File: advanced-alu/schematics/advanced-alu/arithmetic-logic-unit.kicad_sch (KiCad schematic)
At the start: 5 parts

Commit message: updated ALU design
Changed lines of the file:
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@@
     (stroke (width 0) (type default) (color 0 0 0 0))
   )
-  (bus_entry (at 213.36 53.34) (size 2.54 2.54)
-    (stroke (width 0) (type default) (color 0 0 0 0))
-  )
-  (bus_entry (at 210.82 53.34) (size 2.54 2.54)
-    (stroke (width 0) (type default) (color 0 0 0 0))
-  )
-  (bus_entry (at 208.28 53.34) (size 2.54 2.54)
-    (stroke (width 0) (type default) (color 0 0 0 0))
-  )
-  (bus_entry (at 205.74 53.34) (size 2.54 2.54)
-    (stroke (width 0) (type default) (color 0 0 0 0))
-  )
-  (bus_entry (at 146.685 53.34) (size 2.54 2.54)
-    (stroke (width 0) (type default) (color 0 0 0 0))
-  )
-  (bus_entry (at 144.145 53.34) (size 2.54 2.54)
-    (stroke (width 0) (type default) (color 0 0 0 0))
-  )
-  (bus_entry (at 149.225 53.34) (size 2.54 2.54)
-    (stroke (width 0) (type default) (color 0 0 0 0))
-  )
-  (bus_entry (at 151.765 53.34) (size 2.54 2.54)
+  (bus_entry (at 213.36 63.5) (size 2.54 2.54)
+    (stroke (width 0) (type default) (color 0 0 0 0))
+  )
+  (bus_entry (at 210.82 63.5) (size 2.54 2.54)
+    (stroke (width 0) (type default) (color 0 0 0 0))
+  )
+  (bus_entry (at 208.28 63.5) (size 2.54 2.54)
+    (stroke (width 0) (type default) (color 0 0 0 0))
+  )
+  (bus_entry (at 205.74 63.5) (size 2.54 2.54)
+    (stroke (width 0) (type default) (color 0 0 0 0))
+  )
+  (bus_entry (at 146.685 63.5) (size 2.54 2.54)
+    (stroke (width 0) (type default) (color 0 0 0 0))
+  )
+  (bus_entry (at 144.145 63.5) (size 2.54 2.54)
+    (stroke (width 0) (type default) (color 0 0 0 0))
+  )
+  (bus_entry (at 149.225 63.5) (size 2.54 2.54)
+    (stroke (width 0) (type default) (color 0 0 0 0))
+  )
+  (bus_entry (at 151.765 63.5) (size 2.54 2.54)
     (stroke (width 0) (type default) (color 0 0 0 0))
   )
@@
     (stroke (width 0) (type default) (color 0 0 0 0))
   )
-  (bus (pts (xy 151.765 53.34) (xy 205.74 53.34))
+  (bus (pts (xy 151.765 63.5) (xy 205.74 63.5))
     (stroke (width 0) (type default) (color 0 0 0 0))
   )
@@
     (stroke (width 0) (type default) (color 0 0 0 0))
   )
-  (bus (pts (xy 146.685 53.34) (xy 149.225 53.34))
+  (bus (pts (xy 146.685 63.5) (xy 149.225 63.5))
     (stroke (width 0) (type default) (color 0 0 0 0))
   )
@@
     (stroke (width 0) (type default) (color 0 0 0 0))
   )
-  (wire (pts (xy 151.765 55.88) (xy 151.765 84.455))
+  (wire (pts (xy 151.765 66.04) (xy 151.765 84.455))
     (stroke (width 0) (type default) (color 0 0 0 0))
   )
@@
     (stroke (width 0) (type default) (color 0 0 0 0))
   )
-  (bus (pts (xy 208.28 53.34) (xy 210.82 53.34))
+  (bus (pts (xy 208.28 63.5) (xy 210.82 63.5))
     (stroke (width 0) (type default) (color 0 0 0 0))
   )
@@
     (stroke (width 0) (type default) (color 0 0 0 0))
   )
-  (bus (pts (xy 144.145 53.34) (xy 146.685 53.34))
-    (stroke (width 0) (type default) (color 0 0 0 0))
-  )
-  (wire (pts (xy 146.685 55.88) (xy 146.685 84.455))
+  (bus (pts (xy 144.145 63.5) (xy 146.685 63.5))
+    (stroke (width 0) (type default) (color 0 0 0 0))
+  )
+  (wire (pts (xy 146.685 66.04) (xy 146.685 84.455))
     (stroke (width 0) (type default) (color 0 0 0 0))
   )
@@
     (stroke (width 0) (type default) (color 0 0 0 0))
   )
-  (bus (pts (xy 210.82 53.34) (xy 213.36 53.34))
+  (bus (pts (xy 210.82 63.5) (xy 213.36 63.5))
     (stroke (width 0) (type default) (color 0 0 0 0))
   )
@@
     (stroke (width 0) (type default) (color 0 0 0 0))
   )
-  (bus (pts (xy 52.07 53.34) (xy 144.145 53.34))
+  (bus (pts (xy 52.07 63.5) (xy 144.145 63.5))
     (stroke (width 0) (type default) (color 0 0 0 0))
   )
@@
     (stroke (width 0) (type default) (color 0 0 0 0))
   )
-  (wire (pts (xy 210.82 55.88) (xy 210.82 84.455))
+  (wire (pts (xy 210.82 66.04) (xy 210.82 84.455))
     (stroke (width 0) (type default) (color 0 0 0 0))
   )
@@
     (stroke (width 0) (type default) (color 0 0 0 0))
   )
-  (wire (pts (xy 213.36 55.88) (xy 213.36 84.455))
+  (wire (pts (xy 213.36 66.04) (xy 213.36 84.455))
     (stroke (width 0) (type default) (color 0 0 0 0))
   )
@@
     (stroke (width 0) (type default) (color 0 0 0 0))
   )
-  (wire (pts (xy 215.9 55.88) (xy 215.9 84.455))
-    (stroke (width 0) (type default) (color 0 0 0 0))
-  )
-  (bus (pts (xy 205.74 53.34) (xy 208.28 53.34))
+  (wire (pts (xy 215.9 66.04) (xy 215.9 84.455))
+    (stroke (width 0) (type default) (color 0 0 0 0))
+  )
+  (bus (pts (xy 205.74 63.5) (xy 208.28 63.5))
     (stroke (width 0) (type default) (color 0 0 0 0))
   )
@@
     (stroke (width 0) (type default) (color 0 0 0 0))
   )
-  (bus (pts (xy 149.225 53.34) (xy 151.765 53.34))
+  (bus (pts (xy 149.225 63.5) (xy 151.765 63.5))
     (stroke (width 0) (type default) (color 0 0 0 0))
   )
@@
     (stroke (width 0) (type default) (color 0 0 0 0))
   )
-  (wire (pts (xy 208.28 55.88) (xy 208.28 84.455))
+  (wire (pts (xy 208.28 66.04) (xy 208.28 84.455))
     (stroke (width 0) (type default) (color 0 0 0 0))
   )
@@
     (stroke (width 0) (type default) (color 0 0 0 0))
   )
-  (wire (pts (xy 149.225 55.88) (xy 149.225 84.455))
+  (wire (pts (xy 149.225 66.04) (xy 149.225 84.455))
     (stroke (width 0) (type default) (color 0 0 0 0))
   )
@@
     (stroke (width 0) (type default) (color 0 0 0 0))
   )
-  (wire (pts (xy 154.305 55.88) (xy 154.305 84.455))
+  (wire (pts (xy 154.305 66.04) (xy 154.305 84.455))
     (stroke (width 0) (type default) (color 0 0 0 0))
   )
@@
     (effects (font (size 1.27 1.27)) (justify right))
   )
-  (hierarchical_label "LO_TMP_[0..7]" (shape input) (at 52.07 53.34 180)
+  (hierarchical_label "LO_TMP_[0..7]" (shape input) (at 52.07 63.5 180)
     (effects (font (size 1.27 1.27)) (justify right))
   )
@@
       (effects (font (size 1.27 1.27)) hide)
     )
+    (pin "1")
+    (pin "2")
     (pin "3")
     (pin "4")
+    (pin "5")
+    (pin "6")
+    (pin "8")
+    (pin "9")
+    (pin "10")
+    (pin "11")
+    (pin "12")
+    (pin "13")
+    (pin "14")
+    (pin "7")
   )
   (symbol (lib_id "74xx:74LS245") (at 101.6 95.25 270) (mirror x) (unit 1)

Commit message: updated documentation
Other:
- title: (none) -> Advanced Arithmetic Logic Unit - ALU
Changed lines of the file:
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@@
 (kicad_sch (version 20211123) (generator eeschema)
   (paper "A4")
+  (title_block
+    (title "Advanced Arithmetic Logic Unit - ALU")
+  )
   (junction (at 156.21 167.005) (diameter 0) (color 0 0 0 0)
   )

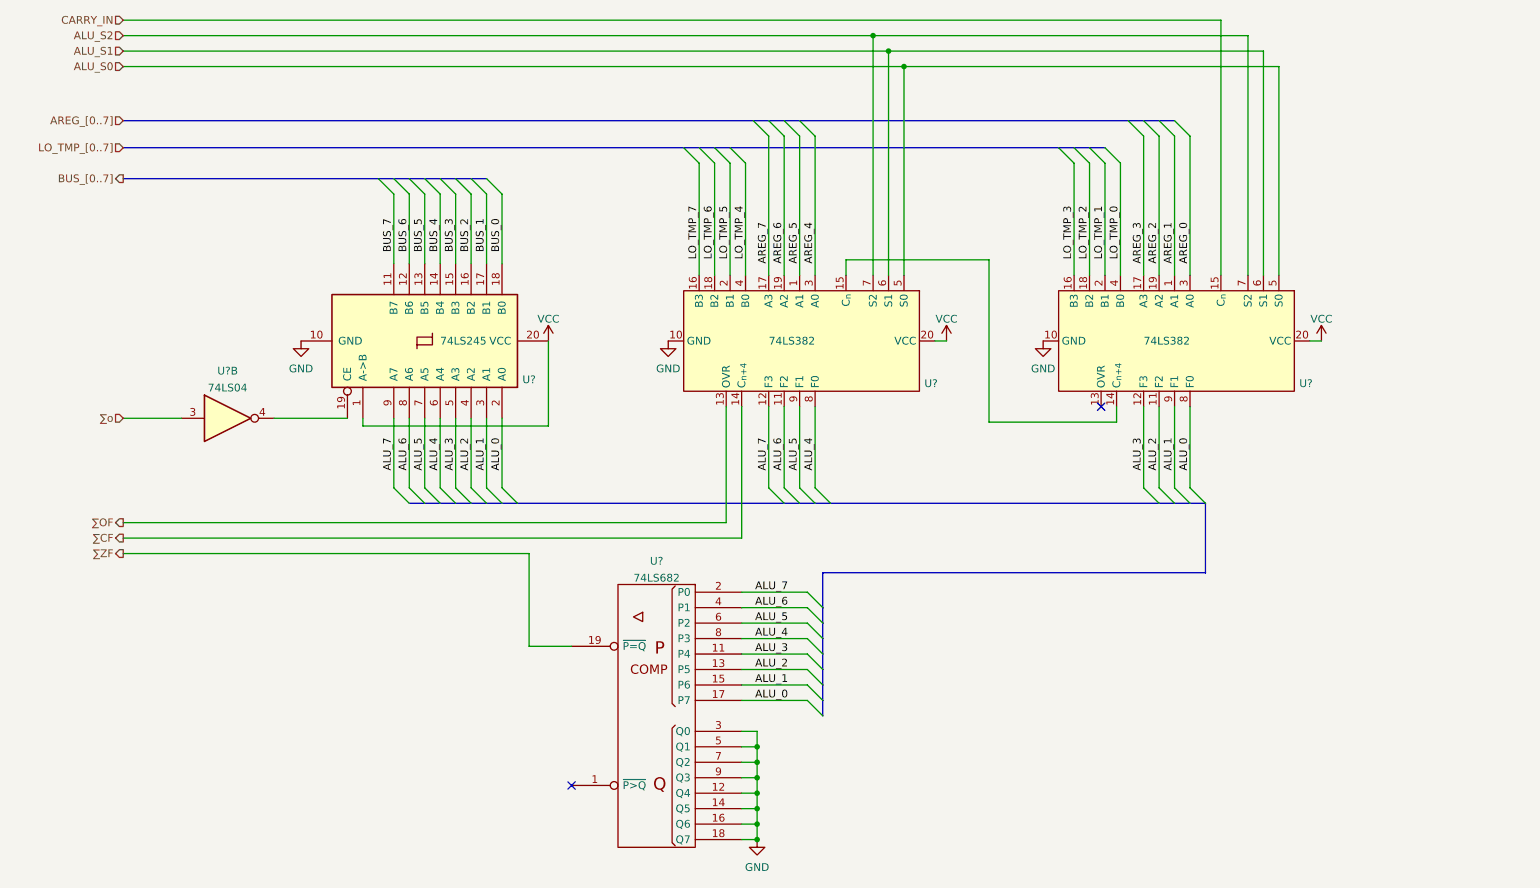
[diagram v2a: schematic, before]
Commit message: returned temp registr to being 8-bit
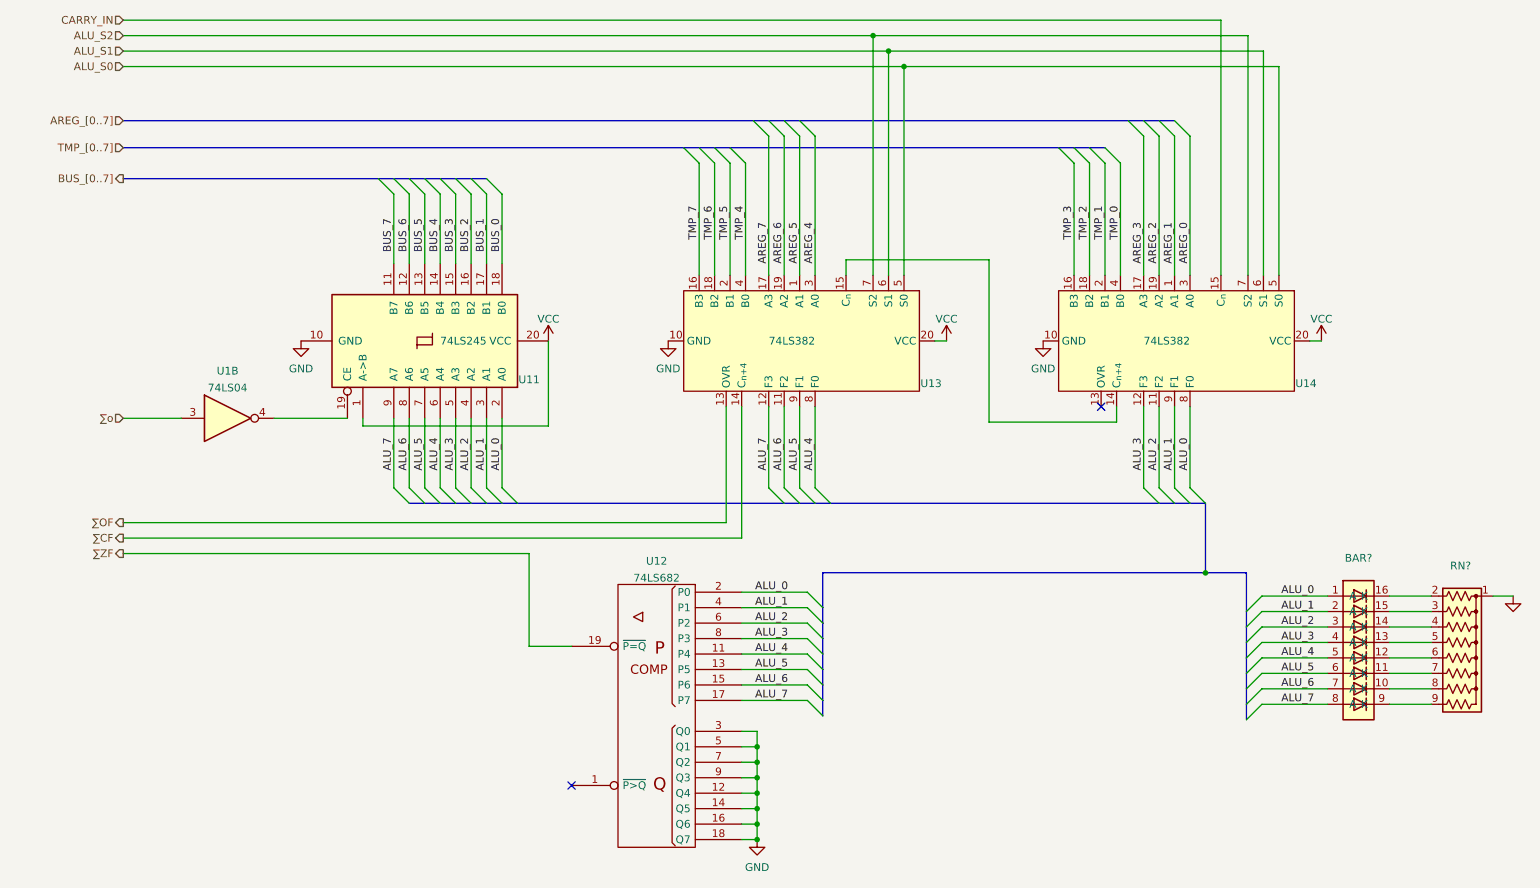
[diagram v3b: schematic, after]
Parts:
- added BAR?: (no value), symbol common-symbols:BarGraphLED_8P
- added RN?: (no value), symbol Device:R_Network08_US
- gave numbers to parts that had none: 5
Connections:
- net ALU_0: now also U12.2 (P0), BAR?.1 (A); no longer U12.17 (P7)
- net ALU_1: now also U12.4 (P1), BAR?.2 (A); no longer U12.15 (P6)
- net ALU_2: now also U12.6 (P2), BAR?.3 (A); no longer U12.13 (P5)
- net ALU_3: now also U12.8 (P3), BAR?.4 (A); no longer U12.11 (P4)
- net ALU_4: now also U12.11 (P4), BAR?.5 (A); no longer U12.8 (P3)
- net ALU_5: now also U12.13 (P5), BAR?.6 (A); no longer U12.6 (P2)
- net ALU_6: now also U12.15 (P6), BAR?.7 (A); no longer U12.4 (P1)
- net ALU_7: now also U12.17 (P7), BAR?.8 (A); no longer U12.2 (P0)
- net GND: now also RN?.1 (common)
- net LO_TMP_0 renamed TMP_0
- net LO_TMP_1 renamed TMP_1
- net LO_TMP_2 renamed TMP_2
- net LO_TMP_3 renamed TMP_3
- net LO_TMP_4 renamed TMP_4
- net LO_TMP_5 renamed TMP_5
- net LO_TMP_6 renamed TMP_6
- net LO_TMP_7 renamed TMP_7
- new net: BAR?.10 (K), RN?.8 (R7)
- new net: BAR?.11 (K), RN?.7 (R6)
- new net: BAR?.12 (K), RN?.6 (R5)
- new net: BAR?.13 (K), RN?.5 (R4)
- new net: BAR?.14 (K), RN?.4 (R3)
- new net: BAR?.15 (K), RN?.3 (R2)
- new net: BAR?.16 (K), RN?.2 (R1)
- new net: BAR?.9 (K), RN?.9 (R8)

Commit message: tweaked design and updated documentation
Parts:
- BAR?: value (none) -> BarGraphLED_8P
- RN?: value (none) -> R_Network08_US; footprint (none) -> Resistor_THT:R_Array_SIP9
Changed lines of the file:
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@@
       (effects (font (size 1.27 1.27)) hide)
     )
-    (property "Value" "" (id 1) (at 280.416 141.6034 0))
+    (property "Value" "GND" (id 1) (at 280.416 141.6034 0))
     (property "Footprint" "" (id 2) (at 280.416 137.16 0)
       (effects (font (size 1.27 1.27)) hide)
@@
     (in_bom yes) (on_board yes) (fields_autoplaced)
     (property "Reference" "BAR?" (id 0) (at 255.016 130.9202 0))
-    (property "Value" "" (id 1) (at 255.016 133.4571 0))
+    (property "Value" "BarGraphLED_8P" (id 1) (at 255.016 133.4571 0))
     (property "Footprint" "" (id 2) (at 255.016 147.32 0)
       (effects (font (size 1.27 1.27)) hide)
@@
     (in_bom yes) (on_board yes) (fields_autoplaced)
     (property "Reference" "RN?" (id 0) (at 271.78 132.1902 90))
-    (property "Value" "" (id 1) (at 271.78 134.7271 90))
-    (property "Footprint" "" (id 2) (at 272.034 159.385 90)
+    (property "Value" "R_Network08_US" (id 1) (at 271.78 134.7271 90))
+    (property "Footprint" "Resistor_THT:R_Array_SIP9" (id 2) (at 272.034 159.385 90)
       (effects (font (size 1.27 1.27)) hide)
     )

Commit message: tweaks and layout improvements
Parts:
- added U12: 74LS04, symbol 74xx:74LS04
- gave numbers to parts that had none: 2
- renumbered U12 to U13, U13 to U14, U14 to U15
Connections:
- net ∑ZF: now also U12.2; no longer U13.19 (~{P=Q})
- new net: U12.1, U13.19 (~{P=Q})
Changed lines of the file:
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@@
+    (stroke (width 0) (type default) (color 0 0 0 0))
+  )
+  (wire (pts (xy 52.07 130.175) (xy 96.52 130.175))
     (stroke (width 0) (type default) (color 0 0 0 0))
   )
@@
     (stroke (width 0) (type default) (color 0 0 0 0))
   )
-  (wire (pts (xy 52.07 130.175) (xy 118.745 130.175))
-    (stroke (width 0) (type default) (color 0 0 0 0))
-  )
   (bus (pts (xy 101.6 68.58) (xy 104.14 68.58))
     (stroke (width 0) (type default) (color 0 0 0 0))
@@
     (stroke (width 0) (type default) (color 0 0 0 0))
   )
+  (wire (pts (xy 96.52 130.175) (xy 96.52 145.415))
+    (stroke (width 0) (type default) (color 0 0 0 0))
+  )
   (bus (pts (xy 160.655 121.92) (xy 163.195 121.92))
     (stroke (width 0) (type default) (color 0 0 0 0))
   )
-  (wire (pts (xy 118.745 145.415) (xy 118.745 130.175))
-    (stroke (width 0) (type default) (color 0 0 0 0))
-  )
   (bus (pts (xy 104.14 68.58) (xy 106.68 68.58))
     (stroke (width 0) (type default) (color 0 0 0 0))
@@
     (stroke (width 0) (type default) (color 0 0 0 0))
   )
-  (wire (pts (xy 125.73 145.415) (xy 118.745 145.415))
+  (wire (pts (xy 125.73 145.415) (xy 125.095 145.415))
     (stroke (width 0) (type default) (color 0 0 0 0))
   )
@@
     (stroke (width 0) (type default) (color 0 0 0 0))
   )
+  (wire (pts (xy 96.52 145.415) (xy 109.855 145.415))
+    (stroke (width 0) (type default) (color 0 0 0 0))
+  )
   (bus (pts (xy 167.005 154.305) (xy 167.005 156.845))
     (stroke (width 0) (type default) (color 0 0 0 0))
@@
   (symbol (lib_id "power:GND") (at 141.605 95.25 0) (unit 1)
     (in_bom yes) (on_board yes) (fields_autoplaced)
-    (property "Reference" "#PWR09" (id 0) (at 141.605 101.6 0)
+    (property "Reference" "#PWR012" (id 0) (at 141.605 101.6 0)
       (effects (font (size 1.27 1.27)) hide)
     )
@@
   (symbol (lib_id "power:VCC") (at 248.92 95.25 0) (unit 1)
     (in_bom yes) (on_board yes) (fields_autoplaced)
-    (property "Reference" "#PWR013" (id 0) (at 248.92 99.06 0)
+    (property "Reference" "#PWR016" (id 0) (at 248.92 99.06 0)
       (effects (font (size 1.27 1.27)) hide)
     )
@@
   (symbol (lib_id "power:GND") (at 203.2 95.25 0) (unit 1)
     (in_bom yes) (on_board yes) (fields_autoplaced)
-    (property "Reference" "#PWR012" (id 0) (at 203.2 101.6 0)
+    (property "Reference" "#PWR015" (id 0) (at 203.2 101.6 0)
       (effects (font (size 1.27 1.27)) hide)
     )
@@
   (symbol (lib_id "power:GND") (at 280.416 137.16 0) (unit 1)
     (in_bom yes) (on_board yes) (fields_autoplaced)
-    (property "Reference" "#PWR?" (id 0) (at 280.416 143.51 0)
+    (property "Reference" "#PWR017" (id 0) (at 280.416 143.51 0)
       (effects (font (size 1.27 1.27)) hide)
     )
@@
   (symbol (lib_id "common-symbols:74LS382") (at 224.79 95.25 270) (unit 1)
     (in_bom yes) (on_board yes)
-    (property "Reference" "U14" (id 0) (at 246.38 102.235 90))
+    (property "Reference" "U15" (id 0) (at 246.38 102.235 90))
     (property "Value" "74LS382" (id 1) (at 223.52 95.25 90))
     (property "Footprint" "" (id 2) (at 220.98 84.455 0)
@@
   (symbol (lib_id "74xx_IEEE:74LS682") (at 139.7 156.845 0) (mirror y) (unit 1)
     (in_bom yes) (on_board yes) (fields_autoplaced)
-    (property "Reference" "U12" (id 0) (at 139.7 131.4155 0))
+    (property "Reference" "U13" (id 0) (at 139.7 131.4155 0))
     (property "Value" "74LS682" (id 1) (at 139.7 134.1906 0))
     (property "Footprint" "" (id 2) (at 139.7 156.845 0)
@@
   (symbol (lib_id "power:VCC") (at 187.325 95.25 0) (unit 1)
     (in_bom yes) (on_board yes) (fields_autoplaced)
-    (property "Reference" "#PWR011" (id 0) (at 187.325 99.06 0)
+    (property "Reference" "#PWR014" (id 0) (at 187.325 99.06 0)
       (effects (font (size 1.27 1.27)) hide)
     )
@@
   (symbol (lib_id "power:GND") (at 156.21 177.165 0) (unit 1)
     (in_bom yes) (on_board yes) (fields_autoplaced)
-    (property "Reference" "#PWR010" (id 0) (at 156.21 183.515 0)
+    (property "Reference" "#PWR013" (id 0) (at 156.21 183.515 0)
       (effects (font (size 1.27 1.27)) hide)
     )
@@
   (symbol (lib_id "power:VCC") (at 121.92 95.25 0) (unit 1)
     (in_bom yes) (on_board yes) (fields_autoplaced)
-    (property "Reference" "#PWR08" (id 0) (at 121.92 99.06 0)
+    (property "Reference" "#PWR011" (id 0) (at 121.92 99.06 0)
       (effects (font (size 1.27 1.27)) hide)
     )
@@
   (symbol (lib_id "common-symbols:BarGraphLED_8P") (at 255.016 147.32 0) (unit 1)
     (in_bom yes) (on_board yes) (fields_autoplaced)
-    (property "Reference" "BAR?" (id 0) (at 255.016 130.9202 0))
+    (property "Reference" "BAR2" (id 0) (at 255.016 130.9202 0))
     (property "Value" "BarGraphLED_8P" (id 1) (at 255.016 133.4571 0))
     (property "Footprint" "" (id 2) (at 255.016 147.32 0)
@@
   (symbol (lib_id "power:GND") (at 81.28 95.25 0) (unit 1)
     (in_bom yes) (on_board yes) (fields_autoplaced)
-    (property "Reference" "#PWR07" (id 0) (at 81.28 101.6 0)
+    (property "Reference" "#PWR010" (id 0) (at 81.28 101.6 0)
       (effects (font (size 1.27 1.27)) hide)
     )
@@
       (effects (font (size 1.27 1.27)) hide)
     )
-    (pin "1")
-    (pin "2")
     (pin "3")
     (pin "4")
-    (pin "5")
-    (pin "6")
-    (pin "8")
-    (pin "9")
-    (pin "10")
-    (pin "11")
-    (pin "12")
-    (pin "13")
-    (pin "14")
-    (pin "7")
+  )
+  (symbol (lib_id "74xx:74LS04") (at 117.475 145.415 180) (unit 1)
+    (in_bom yes) (on_board yes) (fields_autoplaced)
+    (property "Reference" "U12" (id 0) (at 117.475 137.6385 0))
+    (property "Value" "74LS04" (id 1) (at 117.475 140.4136 0))
+    (property "Footprint" "" (id 2) (at 117.475 145.415 0)
+      (effects (font (size 1.27 1.27)) hide)
+    )
+    (property "Datasheet" "http://www.ti.com/lit/gpn/sn74LS04" (id 3) (at 117.475 145.415 0)
+      (effects (font (size 1.27 1.27)) hide)
+    )
+    (pin "1")
+    (pin "2")
   )
   (symbol (lib_id "Device:R_Network08_US") (at 272.034 147.32 270) (unit 1)
     (in_bom yes) (on_board yes) (fields_autoplaced)
-    (property "Reference" "RN?" (id 0) (at 271.78 132.1902 90))
+    (property "Reference" "RN2" (id 0) (at 271.78 132.1902 90))
     (property "Value" "R_Network08_US" (id 1) (at 271.78 134.7271 90))
     (property "Footprint" "Resistor_THT:R_Array_SIP9" (id 2) (at 272.034 159.385 90)
@@
   (symbol (lib_id "common-symbols:74LS382") (at 163.195 95.25 270) (unit 1)
     (in_bom yes) (on_board yes)
-    (property "Reference" "U13" (id 0) (at 184.785 102.235 90))
+    (property "Reference" "U14" (id 0) (at 184.785 102.235 90))
     (property "Value" "74LS382" (id 1) (at 161.925 95.25 90))
     (property "Footprint" "" (id 2) (at 159.385 84.455 0)
